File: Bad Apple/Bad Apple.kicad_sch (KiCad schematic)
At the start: 0 parts

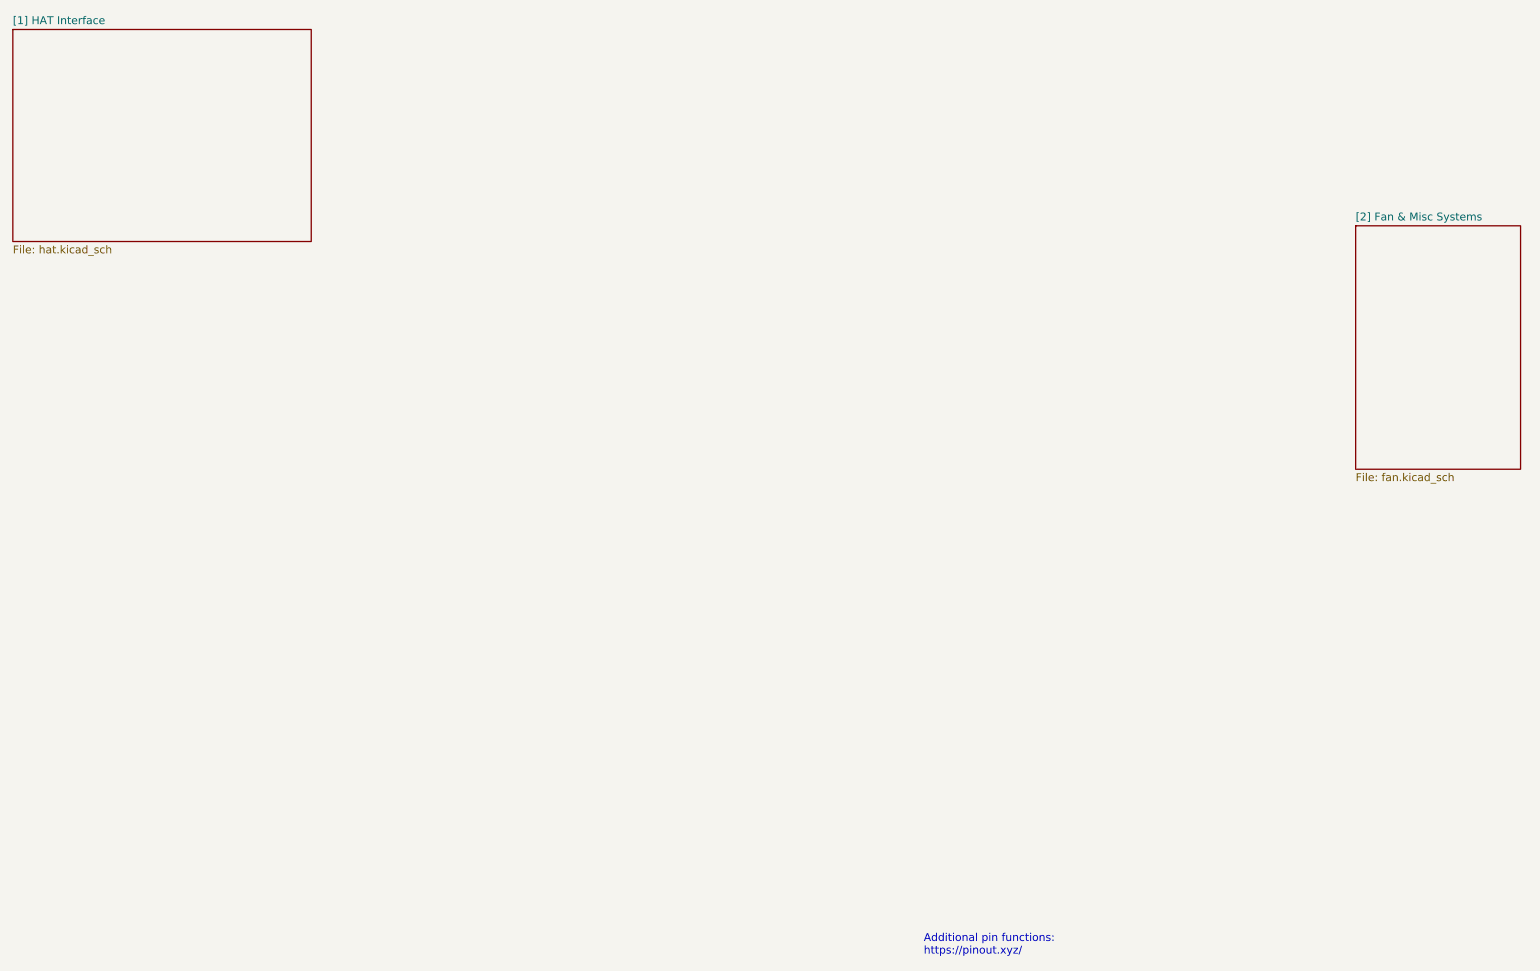
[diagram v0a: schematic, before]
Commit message: chore(pcb): metadata stuff
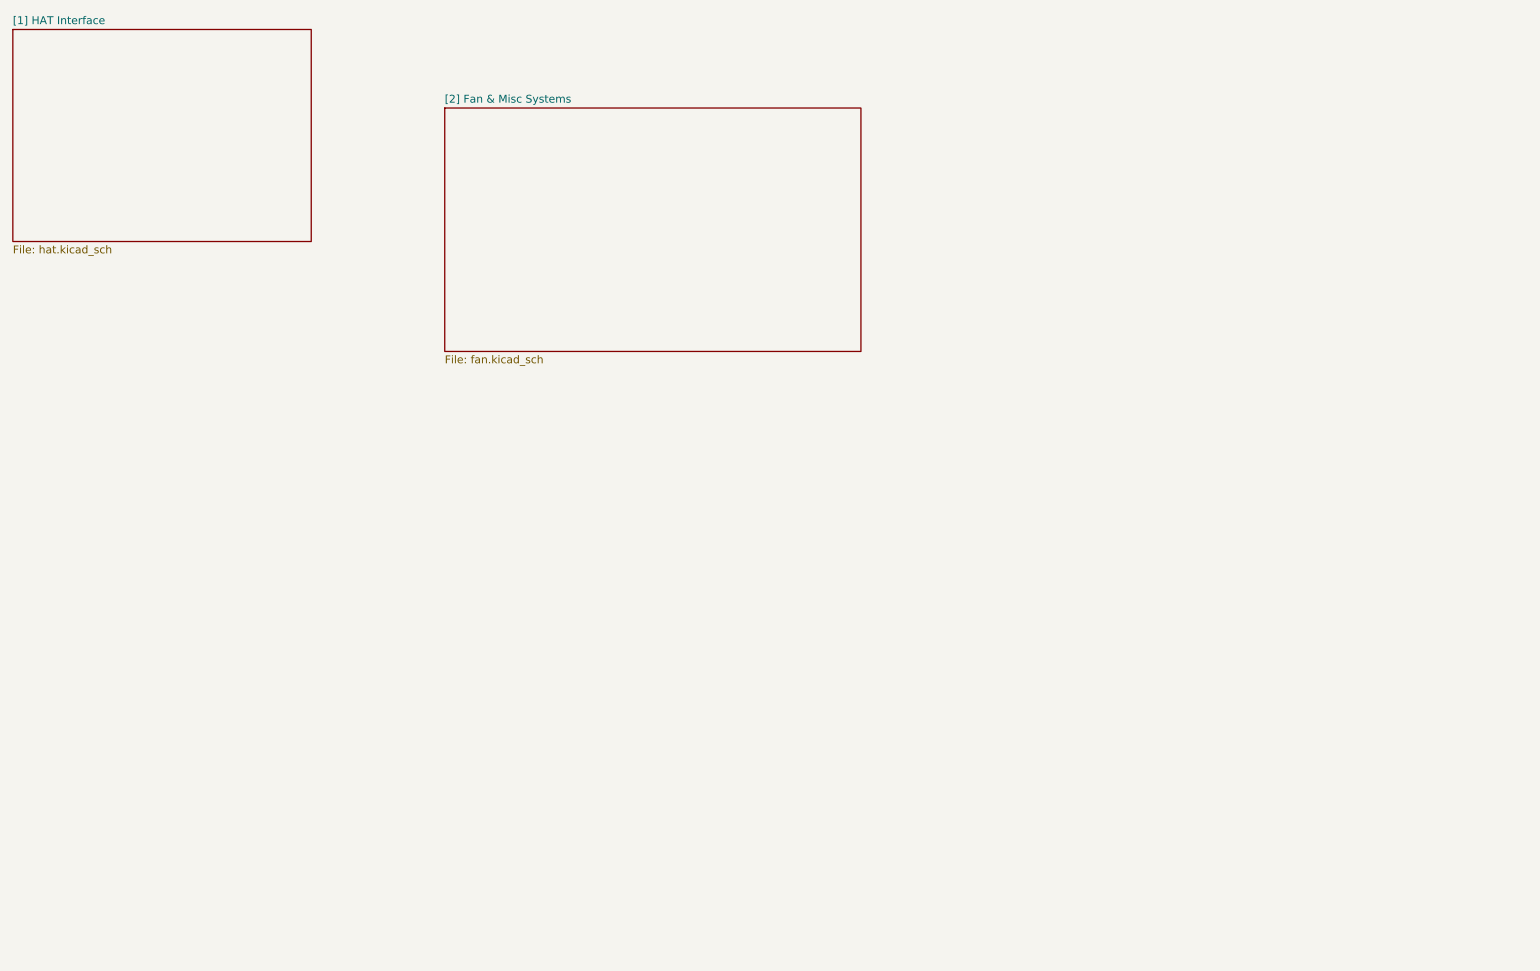
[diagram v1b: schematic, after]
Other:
- note removed: "Additional pin functions: https://pinout.xyz/"
- company: (none) -> Mixed Engineering Group 3 | STEM 12-Altruism / AY 2526 | CIT-U SHS
- title: (none) -> Autonomous  Courier Robot "Bad Apple"
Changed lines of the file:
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@@
 	(paper "A4")
 	(title_block
-		(date "15 nov 2012")
-	)
-	(text "Additional pin functions:\nhttps://pinout.xyz/"
-		(exclude_from_sim no)
-		(at 179.07 180.34 0)
-		(effects
-			(font
-				(size 1.27 1.27)
-			)
-			(justify left bottom)
-		)
+		(title "Autonomous  Courier Robot \"Bad Apple\"")
+		(date "2025-08-28")
+		(rev "1")
+		(company "Mixed Engineering Group 3 | STEM 12-Altruism / AY 2526 | CIT-U SHS")
 	)
 	(sheet
@@
 	)
 	(sheet
-		(at 248.92 62.23)
-		(size 26.67 39.37)
+		(at 101.6 43.18)
+		(size 67.31 39.37)
 		(exclude_from_sim no)
 		(in_bom yes)
@@
 		)
 		(property "Sheetname" "[2] Fan & Misc Systems"
-			(at 248.92 61.5184 0)
+			(at 101.6 42.4684 0)
 			(effects
 				(font
@@
 		)
 		(property "Sheetfile" "fan.kicad_sch"
-			(at 248.92 102.1846 0)
+			(at 101.6 83.1346 0)
 			(effects
 				(font

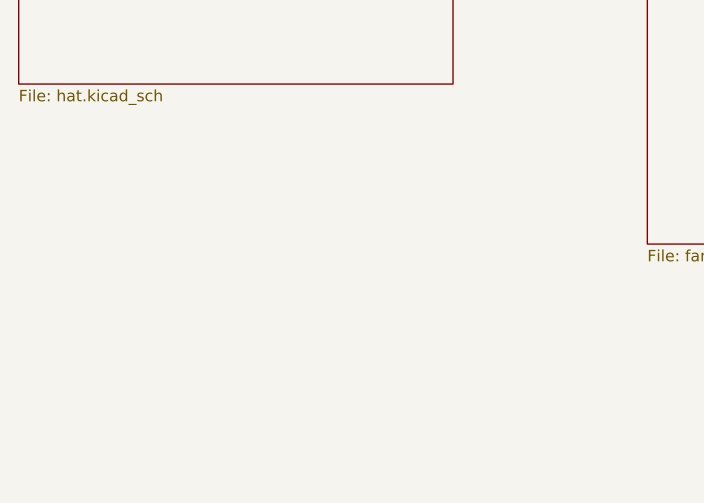
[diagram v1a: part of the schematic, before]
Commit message: feat(pcb):  motor driver subsystem
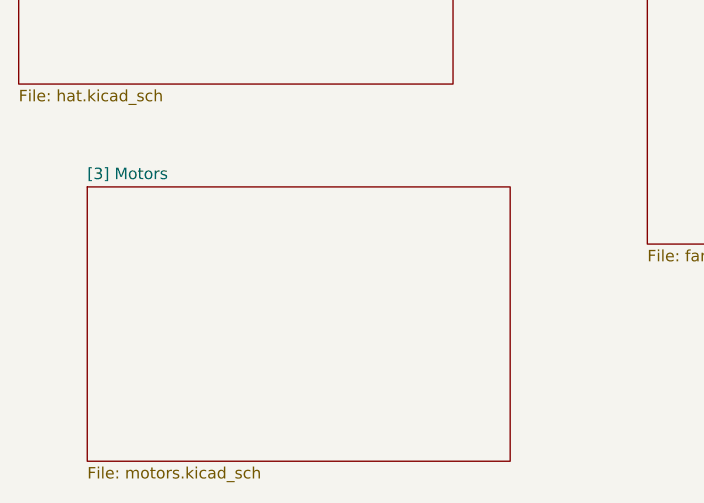
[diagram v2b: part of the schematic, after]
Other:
- added sheet [3] Motors (motors.kicad_sch)
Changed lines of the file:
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@@
 			(project "Bad Apple"
 				(path "/e63e39d7-6ac0-4ffd-8aa3-1841a4541b55"
-					(page "3")
+					(page "2")
 				)
 			)
@@
 				)
 			)
+		)
+	)
+	(sheet
+		(at 39.37 76.2)
+		(size 46.99 30.48)
+		(exclude_from_sim no)
+		(in_bom yes)
+		(on_board yes)
+		(dnp no)
+		(fields_autoplaced yes)
+		(stroke
+			(width 0.1524)
+			(type solid)
+		)
+		(fill
+			(color 0 0 0 0.0000)
+		)
+		(property "Sheetname" "[3] Motors"
+			(at 39.37 75.4884 0)
+			(effects
+				(font
+					(size 1.27 1.27)
+				)
+				(justify left bottom)
+			)
+		)
+		(property "Sheetfile" "motors.kicad_sch"
+			(at 39.37 107.2646 0)
+			(effects
+				(font
+					(size 1.27 1.27)
+				)
+				(justify left top)
+			)
+		)
+		(instances
+			(project "Bad Apple"
+				(path "/e63e39d7-6ac0-4ffd-8aa3-1841a4541b55"
+					(page "4")
+				)
+			)
